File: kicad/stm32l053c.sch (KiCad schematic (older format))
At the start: 51 parts, among them J1 Water_Level, J2 Motion, J3 Door, J4 Door_Led, J5 AIN3, J6 Pump, J7 BATTERY, P1 SWD, Q1 Q_NMOS_GSD, U1 MCP1703A-5002_SOT223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

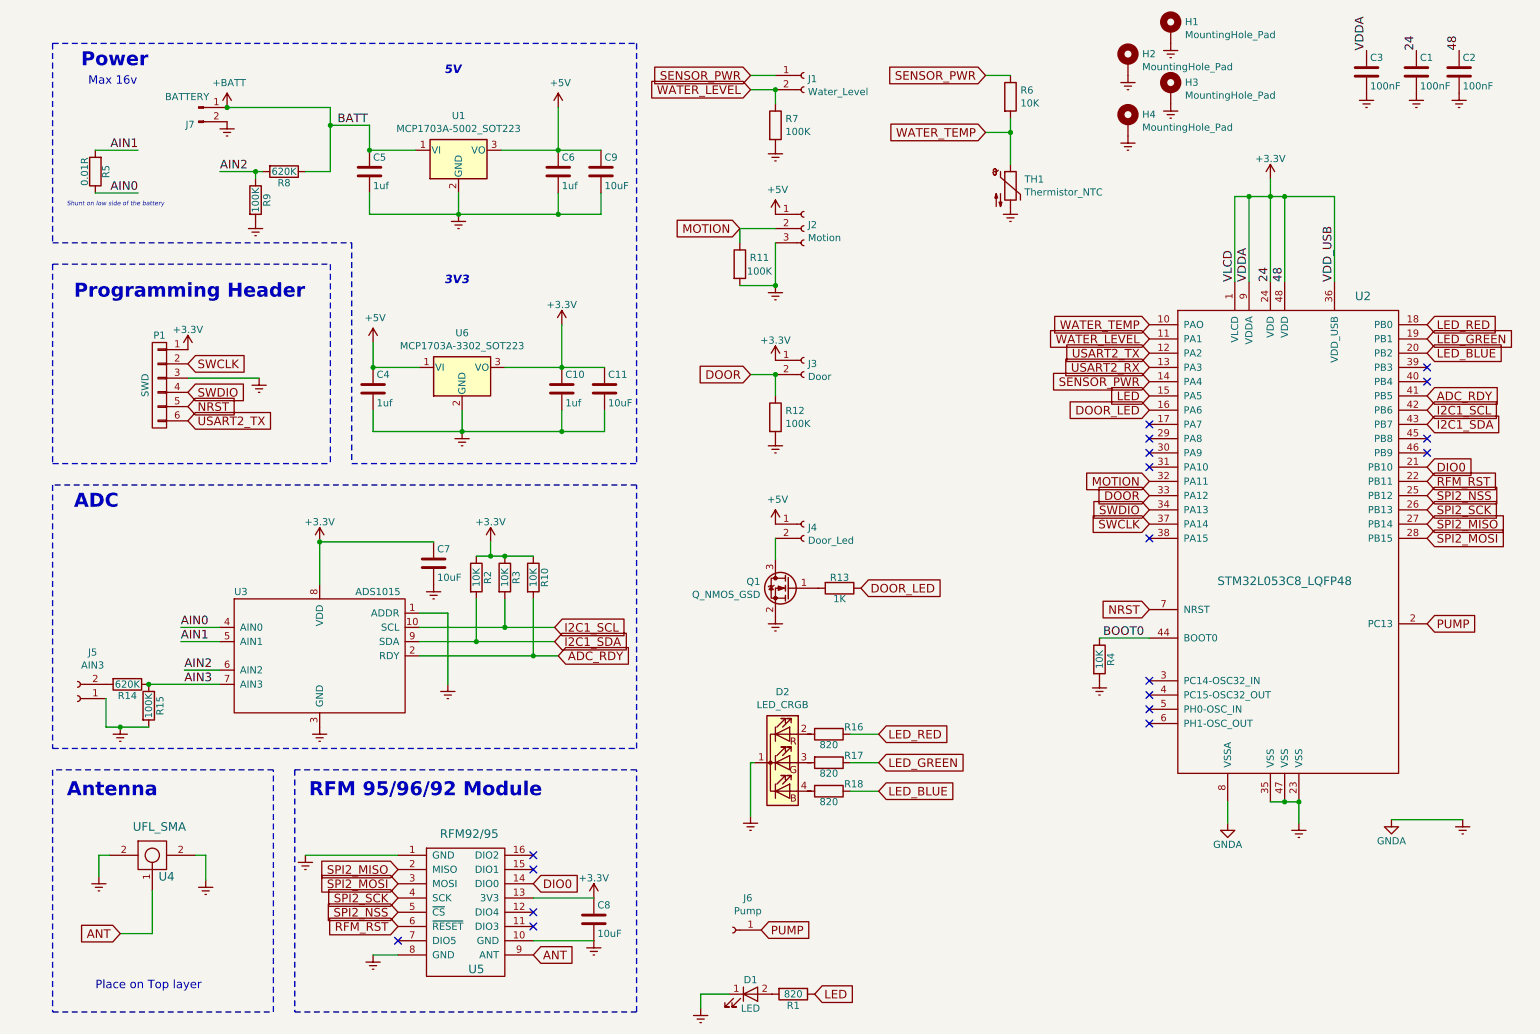
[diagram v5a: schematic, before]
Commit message: Two voltage regulator layout
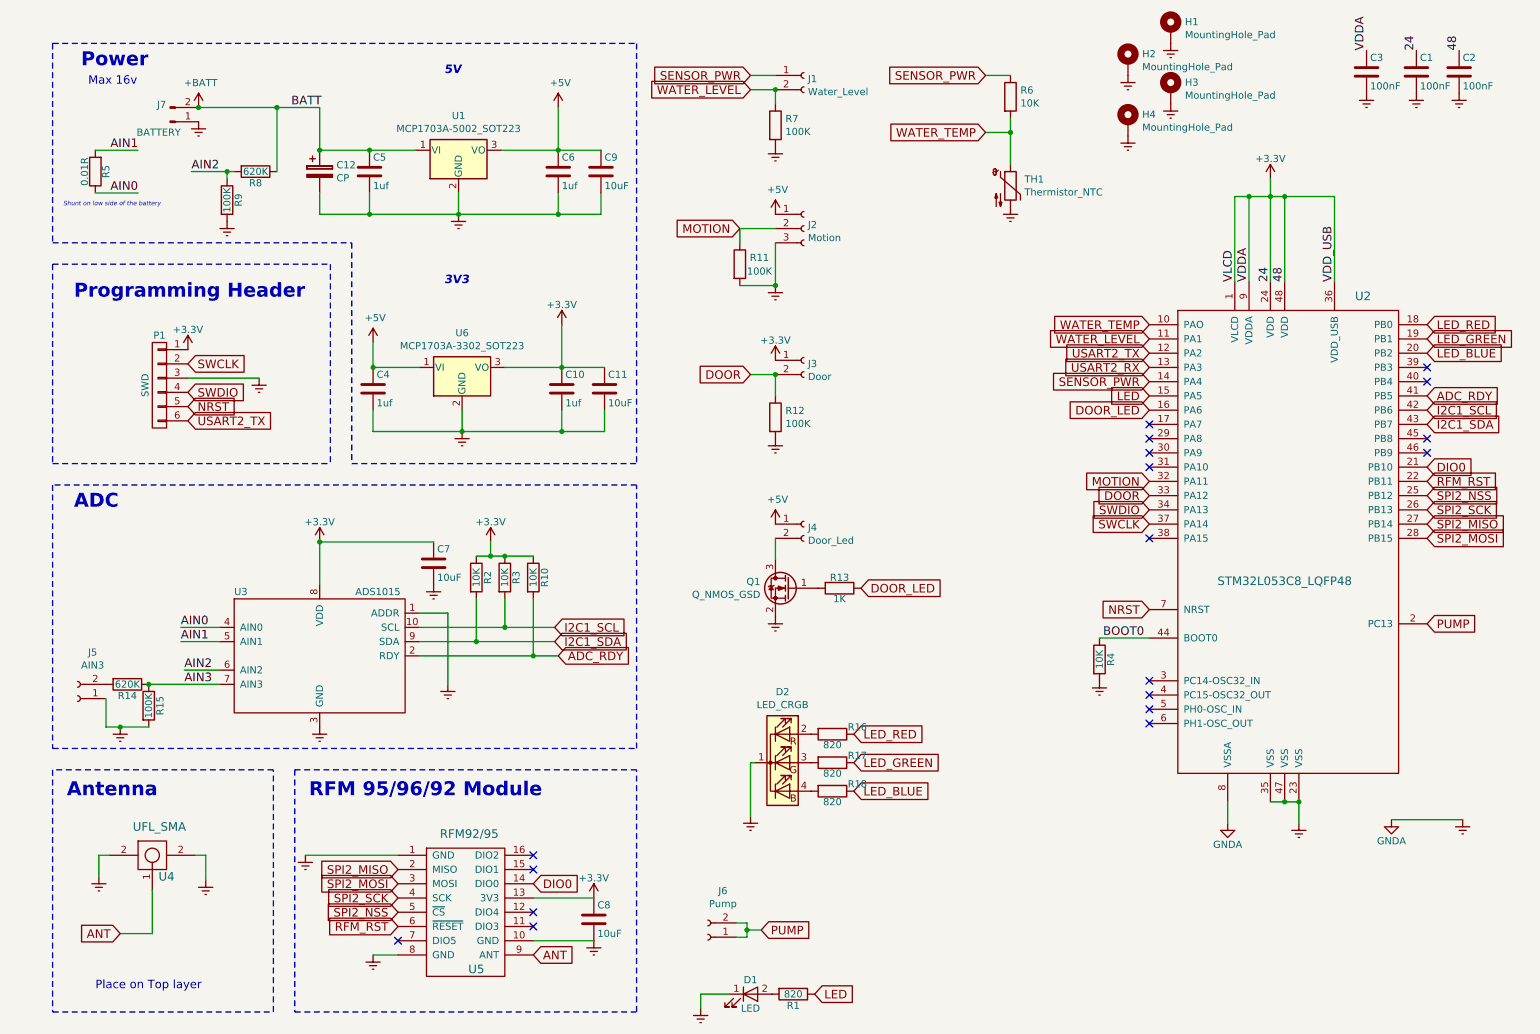
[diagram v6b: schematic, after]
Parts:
- removed J6: Pump, Connector_PinHeader_2.54mm:PinHeader_1x01_P2.54mm_Vertical, symbol Connector:Conn_01x01_Female
- added C12: CP, Capacitor_THT:CP_Radial_D8.0mm_P3.50mm, symbol Device:CP
- added J6: Pump, Connector_JST:JST_XH_B02B-XH-A_1x02_P2.50mm_Vertical, symbol Connector:Conn_01x02_Female
- C1, C10, C11, C2, C3, C4, C5, C6, C7, C8, C9: footprint Capacitors_SMD:C_0805_HandSoldering -> Capacitor_SMD:C_0805_2012Metric_Pad1.15x1.40mm_HandSolder
- J7: footprint Connector_JST:JST_XH_B02B-XH-A_1x02_P2.50mm_Vertical -> TerminalBlock:TerminalBlock_bornier-2_P5.08mm
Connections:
- net +BATT: now also J7.2 (Pin_2), C12.1; no longer J7.1 (Pin_1)
- net Earth: now also J7.1 (Pin_1), C12.2; no longer J7.2 (Pin_2)
- net PUMP: now also J6.1 (Pin_1), J6.2 (Pin_2)
- net at R16.2: now also D2.2 (RA)
- net at R17.2: now also D2.3 (GA)
- net at R18.2: now also D2.4 (BA)
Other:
- moved on the sheet: J7, R16, R17, R18, R8, R9

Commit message: Protection
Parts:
- added D3: 3V6, Diode_THT:D_T-1_P5.08mm_Horizontal, symbol Device:D_Zener
- added F1: Polyfuse, Resistor_SMD:R_1812_4532Metric_Pad1.30x3.40mm_HandSolder, symbol Device:Polyfuse
- added Q2: Q_PMOS_GSD, Package_TO_SOT_SMD:SOT-23_Handsoldering, symbol Device:Q_PMOS_GSD
- added R19, R20, R21: 1K, Resistor_SMD:R_0603_1608Metric_Pad1.05x0.95mm_HandSolder, symbol Device:R
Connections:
- net +3V3: now also D3.1 (K)
- net +BATT: now also Q2.3 (D); no longer C12.1, C5.1, R8.1, U1.1 (VI)
- net AIN0: now also R20.1; no longer R5.1
- net AIN1: now also R19.1; no longer R5.2
- net Earth: now also Q2.1 (G), R21.1; no longer C12.2, C5.2
- new net: C12.1, C5.1, F1.1, U1.1 (VI)
- new net: C12.2, C5.2
- new net: R20.2, R5.1
- new net: R19.2, R5.2
- new net: D3.2 (A), R21.2
- new net BATT: F1.2, Q2.2 (S), R8.1
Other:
- note added: "Paranoia"
- moved on the sheet: C10, C11, C12, C5, C6, C9, J7, R5

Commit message: Solder mask for the ADS1015
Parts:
- U3: footprint Package_SO:TSSOP-10_3x3mm_P0.5mm -> theapi:TSSOP-10_3x3mm_P0.5mm
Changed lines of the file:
@@
 F 0 "U3" H 2250 5475 50  0000 L CNN
 F 1 "ADS1015" H 3100 5475 50  0000 L CNN
-F 2 "Package_SO:TSSOP-10_3x3mm_P0.5mm" H 2800 4975 50  0001 C CNN
+F 2 "theapi:TSSOP-10_3x3mm_P0.5mm" H 2800 4975 50  0001 C CNN
 F 3 "" H 1950 5425 50  0001 C CNN
 	1    2850 5025
